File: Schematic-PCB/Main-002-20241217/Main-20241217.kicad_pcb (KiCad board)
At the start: 4 copper layers, 112 x 112 mm, 98 parts, among them J1 Conn_PWR, J10 Conn_NeoPixel, J11 Conn_Kicker, J12 Conn_LineUART, J2 CamS3-6, J3 CamS3-4, J4 Pixy 2.1, J5 Conn_MD, J6 Conn_Dribbler, J7 Conn_UI, J8 Conn_NeoPixel, J9 Conn_NeoPixel, SW1 SW_DPDT_x2, SW2 Main_RST, SW3 Cam_RST, SW4 Cam_RST, U1 DEV-16771, U10 TSSP4038, U11 TSSP4038, U12 TSSP4038, U13 TSSP4038, U14 TSSP4038, U15 TSSP4038, U16 TSSP4038, U17 TSSP4038, U18 TSSP4038, U3 TSSP4038, U4 TSSP4038, U5 TSSP4038, U6 TSSP4038, U7 TSSP4038, U8 TSSP4038, U9 TSSP4038

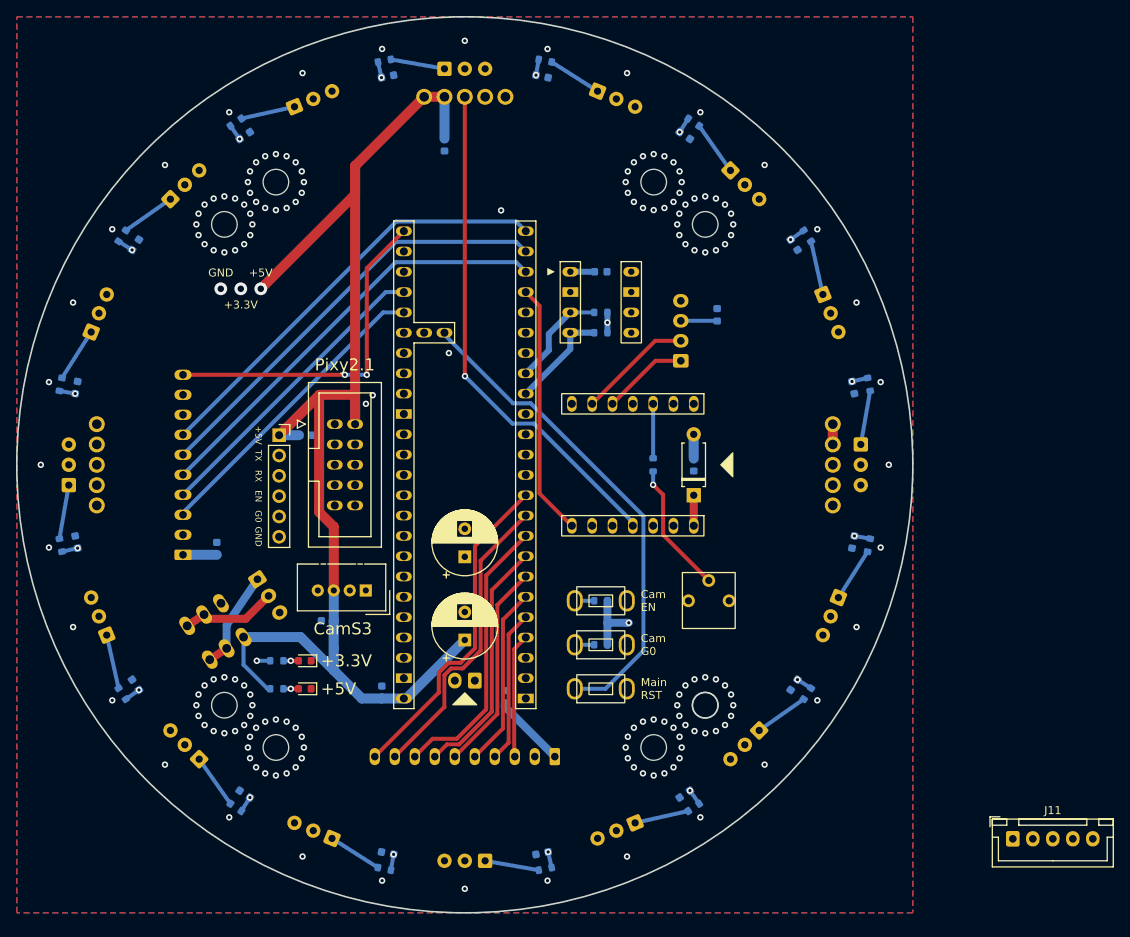
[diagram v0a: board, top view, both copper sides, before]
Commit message: update: メイン基板ver.003 を更新した
キッカー用5ピンも配置した
DRは一通りやったけどそっちでも1回やってみてほしい
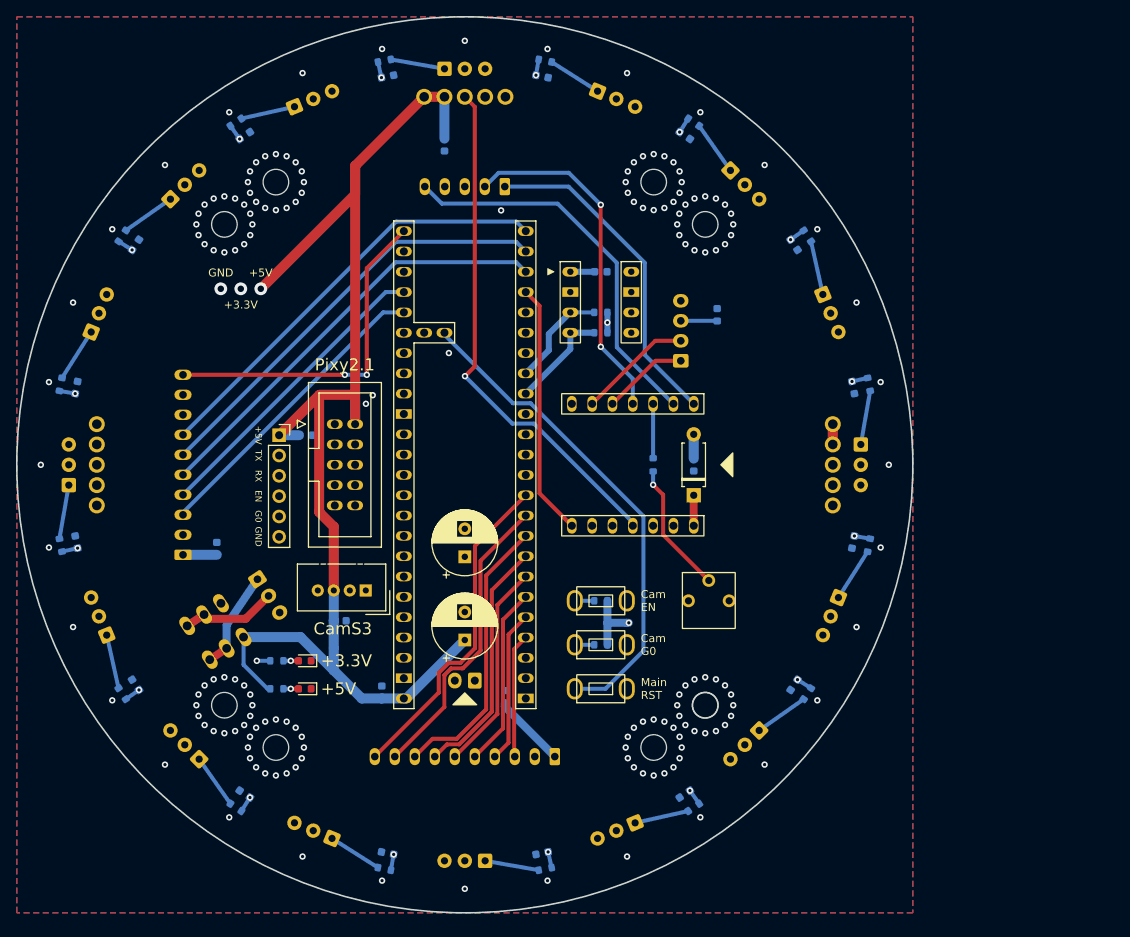
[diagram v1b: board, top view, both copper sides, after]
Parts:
- J11: moved to B.Cu
- moved J11 103.3 mm to (5.00, -34.8), turned to 180 degrees
- moved C7 1.55 mm to (-15.6, 19.5), turned to 0 degrees
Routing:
- net ball02k: track 0.00 -> 48.5 mm
- net KickerSignal: track 0.00 -> 43.4 mm, vias 0 -> 2
- net ball01k: track 0.00 -> 41.6 mm
- net NeoPixel_PWM: track 63.9 -> 64.9 mm
- net ball06: track 45.5 -> 44.7 mm
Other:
- board text added: "Kicker"

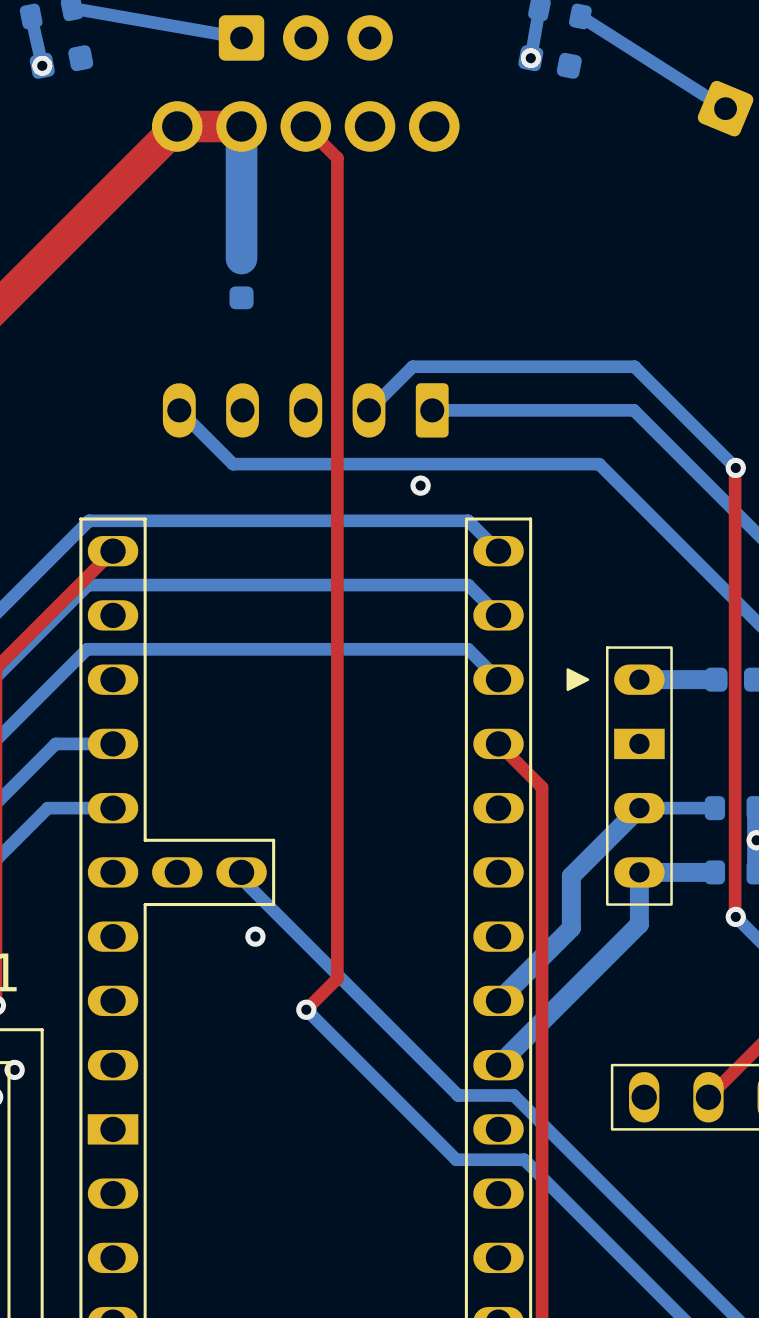
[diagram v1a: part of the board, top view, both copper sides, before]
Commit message: update: メイン基板ver.003のDRをした
特に問題は見つからなかった
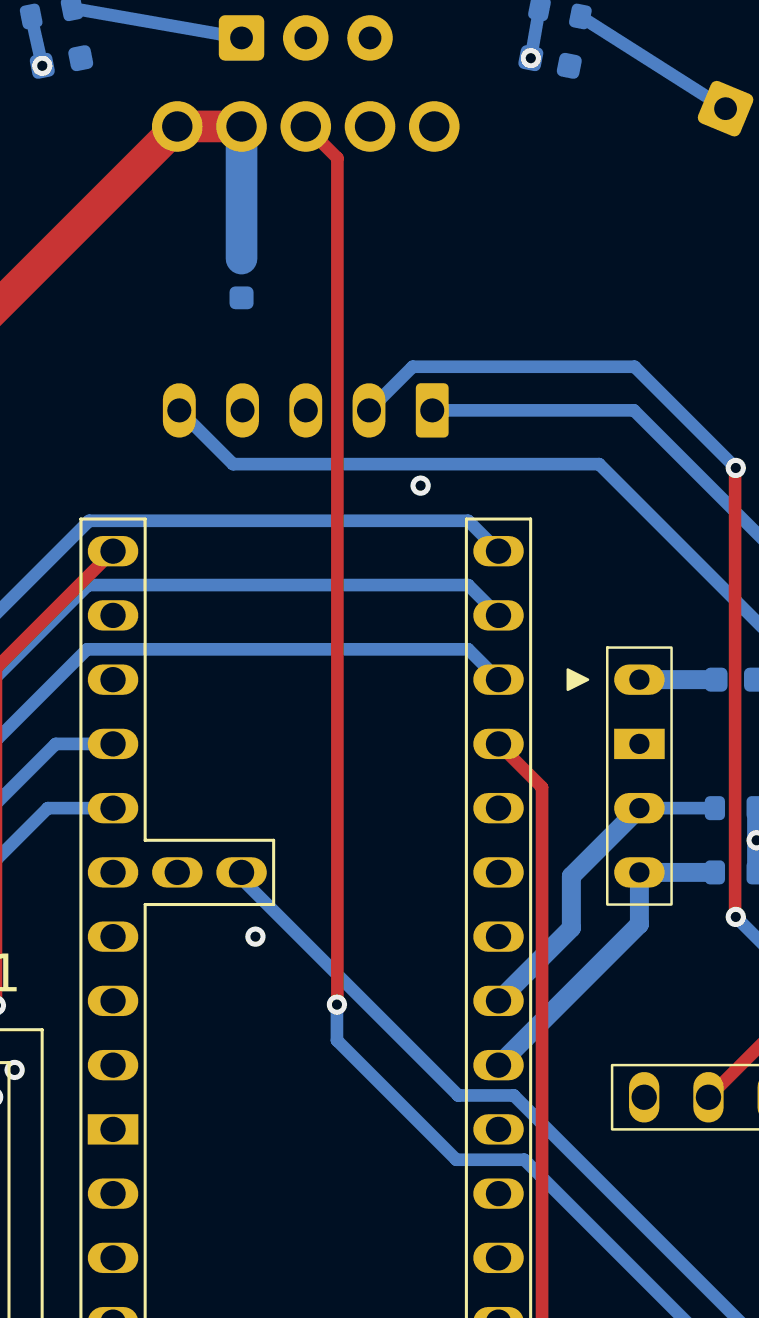
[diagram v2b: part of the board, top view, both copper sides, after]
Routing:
- net NeoPixel_PWM: track 64.9 -> 63.9 mm
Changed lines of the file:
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@@
 		(tags "capacitor")
 		(property "Reference" "C7"
-			(at 0 1.43 360)
+			(at 0 1.43 0)
 			(layer "B.SilkS")
 			(hide yes)
@@
 		)
 		(property "Value" "0.1uF"
-			(at 0 -1.43 360)
+			(at 0 -1.43 0)
 			(layer "B.Fab")
 			(effects
@@
 		)
 		(fp_text user "${REFERENCE}"
-			(at 0 0 360)
+			(at 0 0 0)
 			(layer "B.Fab")
 			(effects
@@
 				(pts
 					(xy 1.657431 31.621871) (xy 1.043404 31.621871) (xy 0.806367 32.531188) (xy 0.570428 31.621871)
-					(xy -0.041767 31.621871) (xy -0.041767 33.1225) (xy 0.339619 33.1225) (xy 0.339619 31.97065) (xy 0.635275 33.1225)
+					(xy -0.041766 31.621871) (xy -0.041766 33.1225) (xy 0.339619 33.1225) (xy 0.339619 31.97065) (xy 0.635275 33.1225)
 					(xy 0.98039 33.1225) (xy 1.275313 31.97065) (xy 1.275313 33.1225) (xy 1.657431 33.1225)
 				)
@@
 			(polygon
 				(pts
-					(xy -0.335224 33.1225) (xy -1.028752 33.1225) (xy -1.076481 33.121057) (xy -1.15189 33.113484)
-					(xy -1.231878 33.099419) (xy -1.306821 33.081467) (xy -1.320823 33.077524) (xy -1.389116 33.050812)
+					(xy -0.335223 33.1225) (xy -1.028751 33.1225) (xy -1.07648 33.121057) (xy -1.151889 33.113484)
+					(xy -1.231877 33.099419) (xy -1.306821 33.081467) (xy -1.320823 33.077524) (xy -1.389116 33.050812)
 					(xy -1.454546 33.012437) (xy -1.517115 32.962398) (xy -1.546637 32.933311) (xy -1.594502 32.875725)
 					(xy -1.635586 32.811415) (xy -1.669888 32.740382) (xy -1.688689 32.686848) (xy -1.705707 32.614788)
 					(xy -1.71743 32.532384) (xy -1.723265 32.45352) (xy -1.724995 32.376582) (xy -1.256263 32.376582)
-					(xy -1.256126 32.398094) (xy -1.252829 32.476588) (xy -1.242526 32.557703) (xy -1.221093 32.630106)
-					(xy -1.182507 32.693041) (xy -1.124373 32.739649) (xy -1.066087 32.758625) (xy -0.991839 32.768327)
-					(xy -0.916278 32.77079) (xy -0.801972 32.77079) (xy -0.801972 31.973581) (xy -0.918476 31.973581)
-					(xy -0.972626 31.975674) (xy -1.048772 31.98773) (xy -1.119001 32.014102) (xy -1.177862 32.05931)
-					(xy -1.187356 32.070553) (xy -1.222499 32.135314) (xy -1.243325 32.212342) (xy -1.253507 32.294768)
+					(xy -1.256126 32.398094) (xy -1.252829 32.476588) (xy -1.242525 32.557703) (xy -1.221092 32.630106)
+					(xy -1.182506 32.693041) (xy -1.124372 32.739649) (xy -1.066086 32.758625) (xy -0.991838 32.768327)
+					(xy -0.916277 32.77079) (xy -0.801971 32.77079) (xy -0.801971 31.973581) (xy -0.918475 31.973581)
+					(xy -0.972625 31.975674) (xy -1.048771 31.98773) (xy -1.119 32.014102) (xy -1.177861 32.05931)
+					(xy -1.187355 32.070553) (xy -1.222498 32.135314) (xy -1.243324 32.212342) (xy -1.253507 32.294768)
 					(xy -1.256263 32.376582) (xy -1.724995 32.376582) (xy -1.725209 32.367056) (xy -1.723909 32.310071)
 					(xy -1.718127 32.235894) (xy -1.706094 32.154907) (xy -1.688207 32.07653) (xy -1.675534 32.034428)
 					(xy -1.647134 31.962838) (xy -1.611546 31.896638) (xy -1.568772 31.835828) (xy -1.541939 31.804714)
 					(xy -1.488229 31.754614) (xy -1.427564 31.712107) (xy -1.359944 31.677192) (xy -1.335556 31.667306)
-					(xy -1.263783 31.645696) (xy -1.182211 31.631002) (xy -1.102795 31.623816) (xy -1.028752 31.621871)
-					(xy -0.335224 31.621871)
+					(xy -1.263783 31.645696) (xy -1.18221 31.631002) (xy -1.102794 31.623816) (xy -1.028751 31.621871)
+					(xy -0.335223 31.621871)
 				)
 			)
@@
 	)
 	(segment
-		(start 1.25 -44.75)
-		(end 0 -46)
+		(start 1.25 -11.3)
+		(end 1.25 -44.75)
 		(width 0.5)
 		(layer "F.Cu")
@@
 	)
 	(segment
-		(start 0.021327 -11.079245)
-		(end 1.25 -12.307918)
+		(start 1.231959 -11.281959)
+		(end 1.25 -11.3)
 		(width 0.5)
 		(layer "F.Cu")
@@
 	)
 	(segment
-		(start 1.25 -12.307918)
-		(end 1.25 -44.75)
+		(start 1.25 -44.75)
+		(end 0 -46)
 		(width 0.5)
 		(layer "F.Cu")
@@
 	)
 	(via
-		(at 0.021327 -11.079245)
+		(at 1.231959 -11.281959)
 		(size 0.8)
 		(drill 0.4)
@@
 	)
 	(segment
-		(start 21 7.207918)
-		(end 21 7.62)
-		(width 0.5)
-		(layer "B.Cu")
-		(net 21)
-	)
-	(segment
-		(start 0.021327 -11.079245)
+		(start 1.231959 -9.868613)
 		(end 5.950572 -5.15)
 		(width 0.5)
@@
 		(width 0.5)
 		(layer "B.Cu")
+		(net 21)
+	)
+	(segment
+		(start 21 7.207918)
+		(end 21 7.62)
+		(width 0.5)
+		(layer "B.Cu")
+		(net 21)
+	)
+	(segment
+		(start 1.231959 -11.281959)
+		(end 1.231959 -9.868613)
+		(width 0.5)
+		(layer "B.Cu")

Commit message: update: メインとMDの基板を編集
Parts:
- added Q1: BSS138, Package_TO_SOT_SMD:SOT-23, F.Cu at (37.3, 50.1)
- added Q2: BSS138, Package_TO_SOT_SMD:SOT-23, F.Cu at (37.3, 54.7)
- added R1: 10k, Resistor_SMD:R_0603_1608Metric, F.Cu at (32.8, 49.0)
- added R2: 10k, Resistor_SMD:R_0603_1608Metric, F.Cu at (32.8, 51.5)
- added R26: 10k, Resistor_SMD:R_0603_1608Metric, F.Cu at (32.8, 54.0)
- added R27: 10k, Resistor_SMD:R_0603_1608Metric, F.Cu at (32.8, 56.5)
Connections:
- J5 pad 10: PH-4 -> EN-2
- J5 pad 3: EN-1 -> PH-3
- J5 pad 4: PH-1 -> EN-3
- J5 pad 5: EN-2 -> PH-4
- J5 pad 6: PH-2 -> EN-4
- J5 pad 7: EN-3 -> PH-1
- J5 pad 8: PH-3 -> EN-1
- J5 pad 9: EN-4 -> PH-2
- U1 pad 2: EN-1 -> PH-3
- U1 pad 3: PH-1 -> EN-3
- U1 pad 4: EN-2 -> PH-4
- U1 pad 5: PH-2 -> EN-4
- U1 pad 6: EN-3 -> PH-1
- U1 pad 7: PH-3 -> EN-1
- U1 pad 8: EN-4 -> PH-2
- U1 pad 9: PH-4 -> EN-2
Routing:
- net PH-3: track 35.1 -> 15.5 mm
- net EN-1: track 15.5 -> 35.1 mm
- net PH-4: track 41.3 -> 22.6 mm
- net EN-2: track 22.6 -> 41.3 mm
- net PH-1: track 19.0 -> 30.6 mm
- net EN-3: track 30.6 -> 19.0 mm
- net PH-2: track 26.2 -> 37.8 mm
- net EN-4: track 37.8 -> 26.2 mm
